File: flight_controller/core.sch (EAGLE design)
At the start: 113 parts, among them J1 MOLEX-2POS, J10 MOLEX-2POS, J11 MOLEX-2POS, J12 MOLEX-2POS, J13 MOLEX-3POS, J14 MOLEX-3POS, J15 MOLEX-4POS, J16 MOLEX-3POS, J17 MOLEX-3POS, J18 MOLEX-3POS, J19 MOLEX-3POS, J2 MOLEX-2POS, J20 MOLEX-4POS, J3 MOLEX-2POS, J4 MOLEX-2POS, J5 MOLEX-2POS, J6 MOLEX-2POS, J7 MOLEX-2POS, J8 MOLEX-2POS, J9 MOLEX-2POS, Q1 MMBT2222A, Q14 MMBT2222A, Q15 MMBT2222A, Q16 MMBT2222A, Q17 MMBT2222A, Q3 MMBT2222A, Q4 MMBT2222A, Q9 MMBT2222A, U1 MPU-6000QFN-24, U2 MEAS-MS5611, U3 USD-SOCKETNEW, U4 STM32F405, U5 MIC5219 3.3V

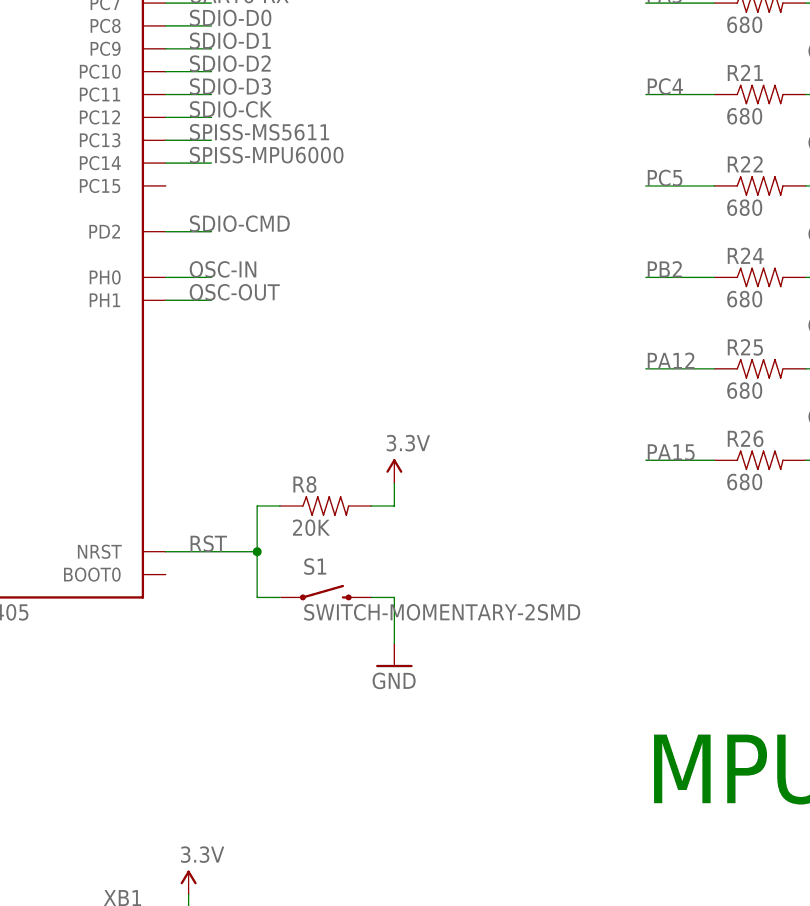
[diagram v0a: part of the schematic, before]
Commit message: Add oscillator.
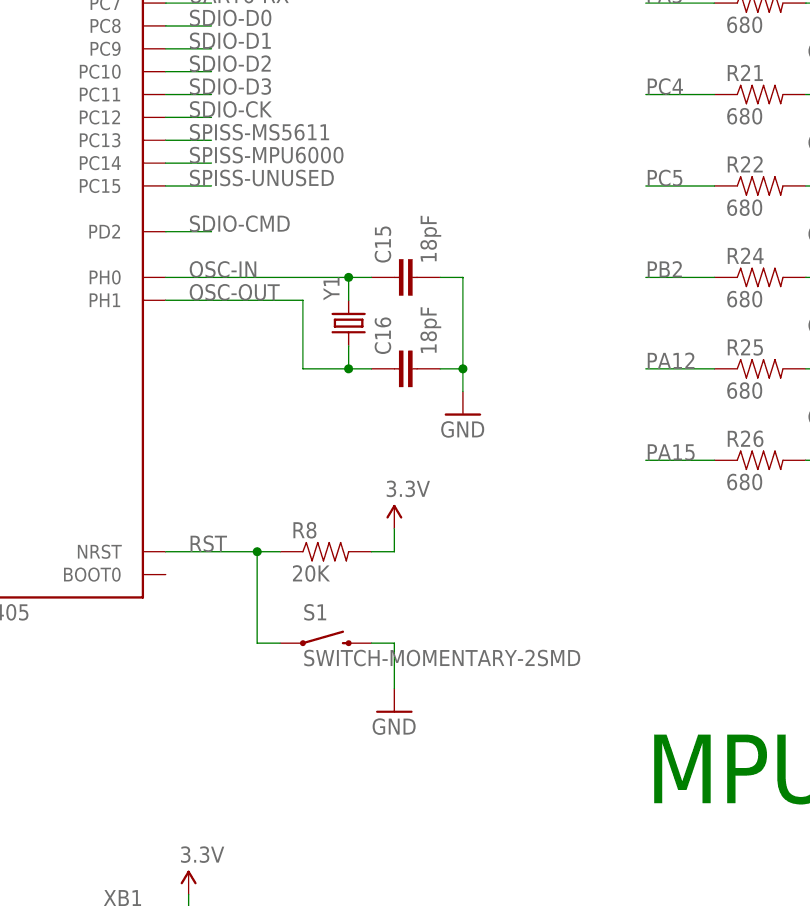
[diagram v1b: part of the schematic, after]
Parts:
- added C15, C16: 18pF, SparkFun-Capacitors:18PF-50V-5%(0603)
- added Y1: (no value), SparkFun-FreqCtrl:CRYSTAL5X3
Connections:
- net GND: now also C15.2, C16.2
- net OSC-IN: now also C15.1, Y1.2
- net OSC-OUT: now also C16.1, Y1.1
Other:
- moved on the sheet: R8, S1
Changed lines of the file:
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@@
 <part name="R37" library="SparkFun-Passives" deviceset="RESISTOR" device="0603-RES" value="20K"/>
 <part name="GND25" library="SparkFun-Aesthetics" deviceset="GND" device=""/>
+<part name="Y1" library="SparkFun-FreqCtrl" deviceset="CRYSTAL" device="5X3"/>
+<part name="C15" library="SparkFun-Capacitors" deviceset="18PF-50V-5%(0603)" device="" value="18pF"/>
+<part name="C16" library="SparkFun-Capacitors" deviceset="18PF-50V-5%(0603)" device="" value="18pF"/>
+<part name="GND26" library="SparkFun-Aesthetics" deviceset="GND" device=""/>
 </parts>
 <sheets>
@@
 <text x="53.34" y="-254" size="7.62" layer="91">MS5611</text>
 <text x="15.24" y="-208.28" size="7.62" layer="91">XBee</text>
-<text x="91.44" y="190.5" size="7.62" layer="98">TODO</text>
 <text x="88.9" y="111.76" size="7.62" layer="98">TODO</text>
 <text x="259.08" y="-523.24" size="7.62" layer="98">TODO</text>
@@
 <instance part="U4" gate=".GPIO" x="60.96" y="203.2"/>
 <instance part="U4" gate=".POWER" x="60.96" y="-154.94"/>
-<instance part="R8" gate="G$1" x="93.98" y="170.18"/>
+<instance part="R8" gate="G$1" x="93.98" y="165.1"/>
 <instance part="C8" gate="G$1" x="81.28" y="-104.14"/>
 <instance part="U5" gate="G$1" x="45.72" y="-91.44"/>
@@
 <instance part="R2" gate="G$1" x="269.24" y="-505.46" rot="R90"/>
 <instance part="SUPPLY16" gate="G$1" x="269.24" y="-474.98"/>
-<instance part="S1" gate="G$1" x="93.98" y="160.02"/>
-<instance part="SUPPLY17" gate="G$1" x="101.6" y="172.72"/>
-<instance part="GND12" gate="1" x="101.6" y="152.4"/>
+<instance part="S1" gate="G$1" x="93.98" y="154.94"/>
+<instance part="SUPPLY17" gate="G$1" x="101.6" y="167.64"/>
+<instance part="GND12" gate="1" x="101.6" y="147.32"/>
 <instance part="GND13" gate="1" x="160.02" y="167.64"/>
 <instance part="GND14" gate="1" x="208.28" y="157.48"/>
@@
 <instance part="R37" gate="G$1" x="177.8" y="-510.54"/>
 <instance part="GND25" gate="1" x="185.42" y="-518.16"/>
+<instance part="Y1" gate="G$1" x="96.52" y="190.5" rot="R90"/>
+<instance part="C15" gate="G$1" x="104.14" y="195.58" rot="R90"/>
+<instance part="C16" gate="G$1" x="104.14" y="185.42" rot="R90"/>
+<instance part="GND26" gate="1" x="109.22" y="180.34"/>
 </instances>
 <busses>
@@
 </segment>
 <segment>
-<wire x1="101.6" y1="160.02" x2="101.6" y2="154.94" width="0.1524" layer="91"/>
+<wire x1="101.6" y1="154.94" x2="101.6" y2="149.86" width="0.1524" layer="91"/>
 <pinref part="S1" gate="G$1" pin="2"/>
-<wire x1="101.6" y1="160.02" x2="99.06" y2="160.02" width="0.1524" layer="91"/>
+<wire x1="101.6" y1="154.94" x2="99.06" y2="154.94" width="0.1524" layer="91"/>
 <pinref part="GND12" gate="1" pin="GND"/>
 </segment>
@@
 <junction x="185.42" y="-510.54"/>
 </segment>
+<segment>
+<pinref part="C15" gate="G$1" pin="2"/>
+<pinref part="GND26" gate="1" pin="GND"/>
+<wire x1="106.68" y1="195.58" x2="109.22" y2="195.58" width="0.1524" layer="91"/>
+<wire x1="109.22" y1="195.58" x2="109.22" y2="185.42" width="0.1524" layer="91"/>
+<pinref part="C16" gate="G$1" pin="2"/>
+<wire x1="109.22" y1="185.42" x2="109.22" y2="182.88" width="0.1524" layer="91"/>
+<wire x1="106.68" y1="185.42" x2="109.22" y2="185.42" width="0.1524" layer="91"/>
+<junction x="109.22" y="185.42"/>
+</segment>
 </net>
 <net name="UART4-TX" class="0">
@@
 <wire x1="86.36" y1="165.1" x2="76.2" y2="165.1" width="0.1524" layer="91"/>
 <label x="78.74" y="165.1" size="1.778" layer="95"/>
-<wire x1="86.36" y1="170.18" x2="86.36" y2="165.1" width="0.1524" layer="91"/>
 <pinref part="S1" gate="G$1" pin="1"/>
-<wire x1="86.36" y1="165.1" x2="86.36" y2="160.02" width="0.1524" layer="91"/>
-<wire x1="86.36" y1="160.02" x2="88.9" y2="160.02" width="0.1524" layer="91"/>
+<wire x1="86.36" y1="165.1" x2="86.36" y2="154.94" width="0.1524" layer="91"/>
+<wire x1="86.36" y1="154.94" x2="88.9" y2="154.94" width="0.1524" layer="91"/>
 <junction x="86.36" y="165.1"/>
 <pinref part="R8" gate="G$1" pin="1"/>
-<wire x1="88.9" y1="170.18" x2="86.36" y2="170.18" width="0.1524" layer="91"/>
+<wire x1="88.9" y1="165.1" x2="86.36" y2="165.1" width="0.1524" layer="91"/>
 </segment>
 </net>
@@
 <segment>
 <pinref part="SUPPLY17" gate="G$1" pin="3.3V"/>
-<wire x1="101.6" y1="170.18" x2="101.6" y2="172.72" width="0.1524" layer="91"/>
+<wire x1="101.6" y1="165.1" x2="101.6" y2="167.64" width="0.1524" layer="91"/>
 <pinref part="R8" gate="G$1" pin="2"/>
-<wire x1="99.06" y1="170.18" x2="101.6" y2="170.18" width="0.1524" layer="91"/>
+<wire x1="99.06" y1="165.1" x2="101.6" y2="165.1" width="0.1524" layer="91"/>
 </segment>
 <segment>
@@
 <net name="OSC-IN" class="0">
 <segment>
-<wire x1="76.2" y1="195.58" x2="81.28" y2="195.58" width="0.1524" layer="91"/>
 <label x="78.74" y="195.58" size="1.778" layer="95"/>
 <pinref part="U4" gate=".GPIO" pin="PH0"/>
+<wire x1="76.2" y1="195.58" x2="96.52" y2="195.58" width="0.1524" layer="91"/>
+<pinref part="C15" gate="G$1" pin="1"/>
+<pinref part="Y1" gate="G$1" pin="2"/>
+<wire x1="96.52" y1="195.58" x2="99.06" y2="195.58" width="0.1524" layer="91"/>
+<wire x1="96.52" y1="193.04" x2="96.52" y2="195.58" width="0.1524" layer="91"/>
+<junction x="96.52" y="195.58"/>
 </segment>
 </net>
 <net name="OSC-OUT" class="0">
 <segment>
-<wire x1="76.2" y1="193.04" x2="81.28" y2="193.04" width="0.1524" layer="91"/>
 <label x="78.74" y="193.04" size="1.778" layer="95"/>
 <pinref part="U4" gate=".GPIO" pin="PH1"/>
+<wire x1="76.2" y1="193.04" x2="91.44" y2="193.04" width="0.1524" layer="91"/>
+<wire x1="91.44" y1="193.04" x2="91.44" y2="185.42" width="0.1524" layer="91"/>
+<wire x1="91.44" y1="185.42" x2="96.52" y2="185.42" width="0.1524" layer="91"/>
+<pinref part="C16" gate="G$1" pin="1"/>
+<pinref part="Y1" gate="G$1" pin="1"/>
+<wire x1="96.52" y1="185.42" x2="99.06" y2="185.42" width="0.1524" layer="91"/>
+<wire x1="96.52" y1="185.42" x2="96.52" y2="187.96" width="0.1524" layer="91"/>
+<junction x="96.52" y="185.42"/>
 </segment>
 </net>
@@
 </segment>
 </net>
+<net name="SPISS-UNUSED" class="0">
+<segment>
+<wire x1="76.2" y1="205.74" x2="81.28" y2="205.74" width="0.1524" layer="91"/>
+<label x="78.74" y="205.74" size="1.778" layer="95"/>
+</segment>
+</net>

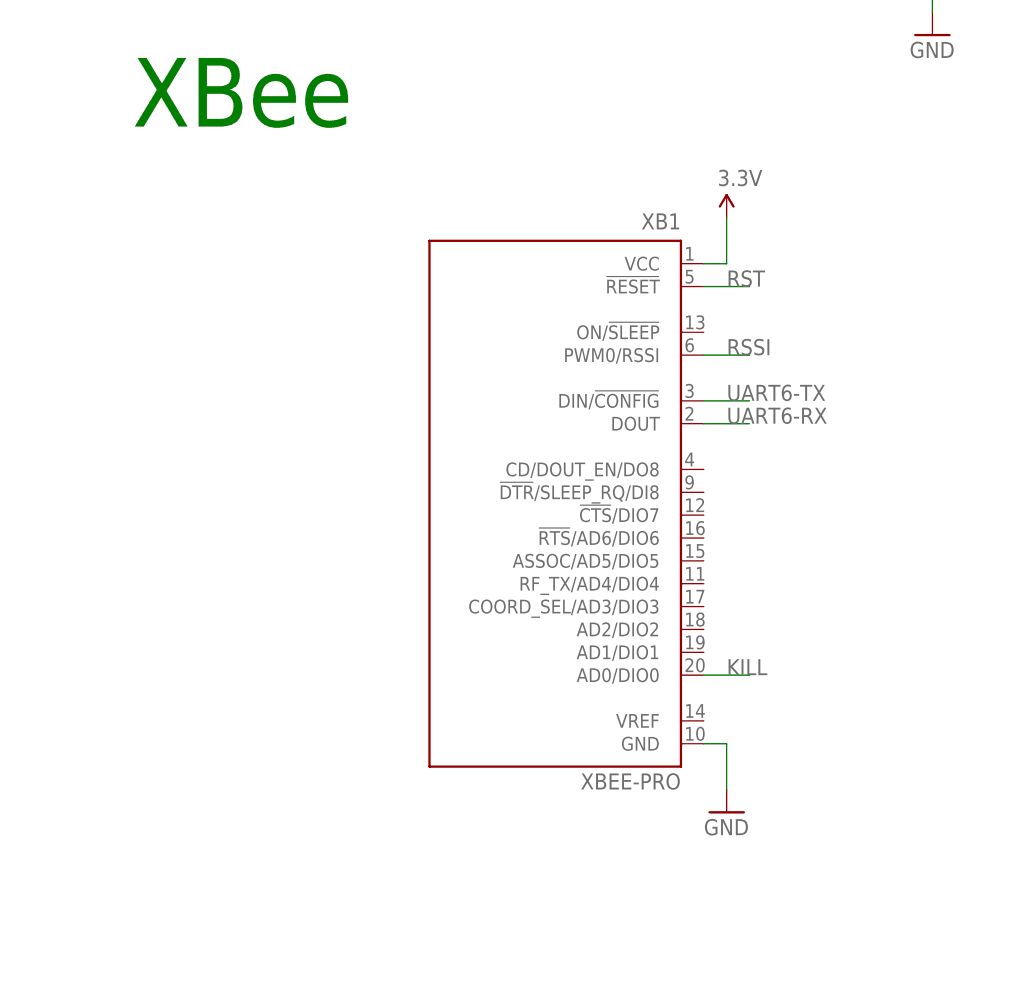
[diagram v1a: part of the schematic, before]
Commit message: Replace XBee headers with SMD variant.
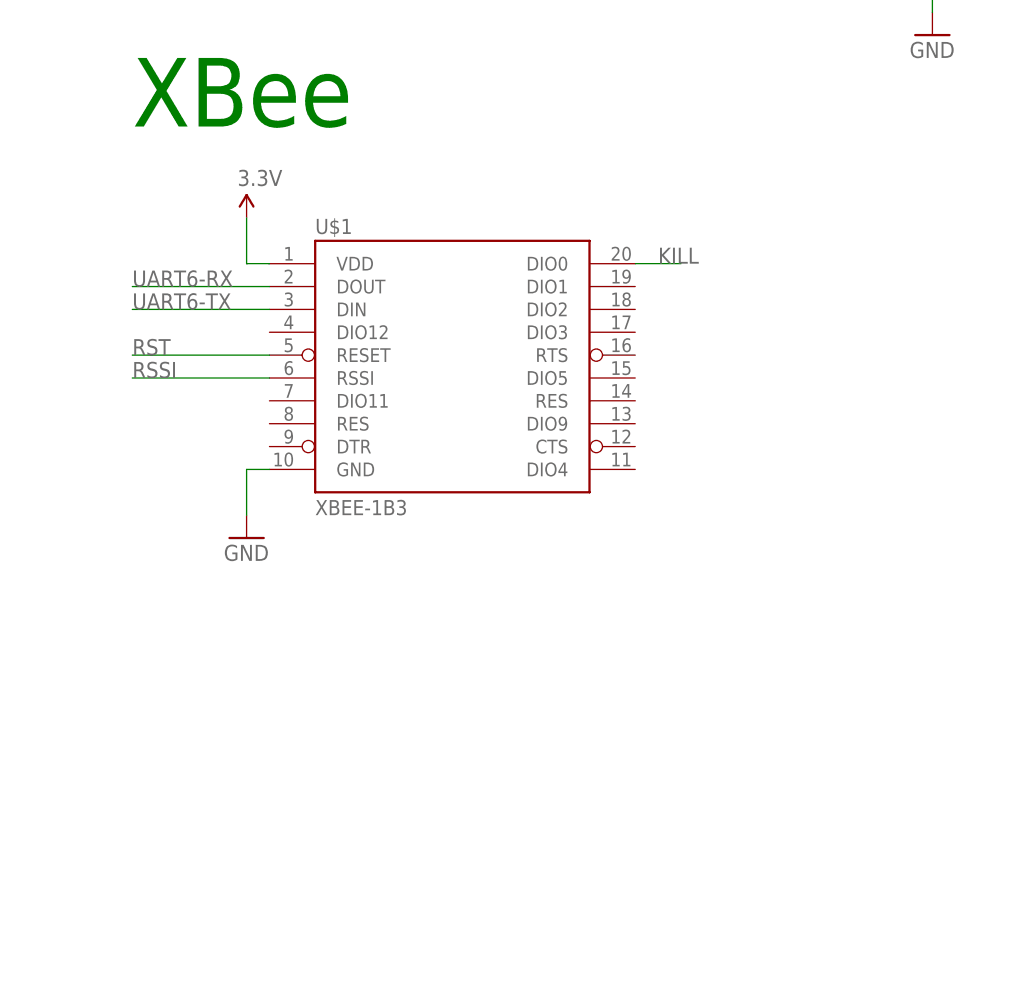
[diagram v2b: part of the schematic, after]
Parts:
- removed XB1: XBEE-PRO, maxstream:XBEE-PRO
- added U$1: XBEE-1B3, SparkFun-RF:XBEE-1B3
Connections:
- net 3.3V: now also U$1.VDD; no longer XB1.VCC
- net GND: now also U$1.GND; no longer XB1.GND
- net KILL: now also U$1.DIO0; no longer XB1.AD0/DIO0
- net RSSI: now also U$1.RSSI; no longer XB1.PWM0/RSSI
- net RST: now also U$1.RESET; no longer XB1.!RESET
- net UART6-RX: now also U$1.DOUT; no longer XB1.DOUT
- net UART6-TX: now also U$1.DIN; no longer XB1.DIN/!CONFIG
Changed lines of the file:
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@@
 </classes>
 <parts>
-<part name="XB1" library="maxstream" deviceset="XBEE" device="-PRO"/>
 <part name="SUPPLY1" library="SparkFun-Aesthetics" deviceset="3.3V" device=""/>
 <part name="GND1" library="SparkFun-Aesthetics" deviceset="GND" device=""/>
-<part name="SUPPLY3" library="SparkFun-Aesthetics" deviceset="3.3V" device=""/>
 <part name="GND2" library="SparkFun-Aesthetics" deviceset="GND" device=""/>
-<part name="GND3" library="SparkFun-Aesthetics" deviceset="GND" device=""/>
 <part name="SUPPLY4" library="SparkFun-Aesthetics" deviceset="5V" device=""/>
 <part name="GND4" library="SparkFun-Aesthetics" deviceset="GND" device=""/>
@@
 <part name="C16" library="SparkFun-Capacitors" deviceset="18PF-50V-5%(0603)" device="" value="18pF"/>
 <part name="GND26" library="SparkFun-Aesthetics" deviceset="GND" device=""/>
+<part name="U$1" library="SparkFun-RF" deviceset="XBEE-1" device="B3"/>
+<part name="GND27" library="SparkFun-Aesthetics" deviceset="GND" device=""/>
+<part name="SUPPLY11" library="SparkFun-Aesthetics" deviceset="3.3V" device=""/>
 </parts>
 <sheets>
@@
 </plain>
 <instances>
-<instance part="XB1" gate="G$1" x="60.96" y="96.52" rot="MR0"/>
 <instance part="SUPPLY1" gate="G$1" x="17.78" y="-144.78"/>
 <instance part="GND1" gate="1" x="60.96" y="-182.88"/>
-<instance part="SUPPLY3" gate="G$1" x="78.74" y="127"/>
 <instance part="GND2" gate="1" x="187.96" y="-447.04"/>
-<instance part="GND3" gate="1" x="78.74" y="60.96"/>
 <instance part="SUPPLY4" gate="G$1" x="187.96" y="-414.02"/>
 <instance part="GND4" gate="1" x="33.02" y="-482.6"/>
@@
 <instance part="C16" gate="G$1" x="104.14" y="185.42" rot="R90"/>
 <instance part="GND26" gate="1" x="109.22" y="180.34"/>
+<instance part="U$1" gate="G$1" x="48.26" y="111.76"/>
+<instance part="GND27" gate="1" x="25.4" y="91.44"/>
+<instance part="SUPPLY11" gate="G$1" x="25.4" y="127"/>
 </instances>
 <busses>
@@
 <label x="213.36" y="-416.56" size="1.778" layer="95"/>
 <pinref part="J20" gate="G$1" pin="2"/>
-</segment>
-<segment>
-<pinref part="XB1" gate="G$1" pin="GND"/>
-<wire x1="76.2" y1="68.58" x2="78.74" y2="68.58" width="0.1524" layer="91"/>
-<wire x1="78.74" y1="68.58" x2="78.74" y2="63.5" width="0.1524" layer="91"/>
-<pinref part="GND3" gate="1" pin="GND"/>
 </segment>
 <segment>
@@
 <junction x="109.22" y="185.42"/>
 </segment>
+<segment>
+<pinref part="U$1" gate="G$1" pin="GND"/>
+<wire x1="27.94" y1="99.06" x2="25.4" y2="99.06" width="0.1524" layer="91"/>
+<wire x1="25.4" y1="99.06" x2="25.4" y2="93.98" width="0.1524" layer="91"/>
+<pinref part="GND27" gate="1" pin="GND"/>
+</segment>
 </net>
 <net name="UART4-TX" class="0">
@@
 <label x="213.36" y="-414.02" size="1.778" layer="95"/>
 <pinref part="J20" gate="G$1" pin="1"/>
-</segment>
-<segment>
-<pinref part="XB1" gate="G$1" pin="!RESET"/>
-<wire x1="76.2" y1="119.38" x2="81.28" y2="119.38" width="0.1524" layer="91"/>
-<label x="78.74" y="119.38" size="1.778" layer="95"/>
 </segment>
 <segment>
@@
 <pinref part="R8" gate="G$1" pin="1"/>
 <wire x1="88.9" y1="165.1" x2="86.36" y2="165.1" width="0.1524" layer="91"/>
+</segment>
+<segment>
+<pinref part="U$1" gate="G$1" pin="RESET"/>
+<wire x1="27.94" y1="111.76" x2="12.7" y2="111.76" width="0.1524" layer="91"/>
+<label x="12.7" y="111.76" size="1.778" layer="95"/>
 </segment>
 </net>
@@
 </segment>
 <segment>
-<pinref part="XB1" gate="G$1" pin="VCC"/>
-<wire x1="76.2" y1="121.92" x2="78.74" y2="121.92" width="0.1524" layer="91"/>
-<wire x1="78.74" y1="121.92" x2="78.74" y2="127" width="0.1524" layer="91"/>
-<pinref part="SUPPLY3" gate="G$1" pin="3.3V"/>
-</segment>
-<segment>
 <wire x1="193.04" y1="-436.88" x2="187.96" y2="-436.88" width="0.1524" layer="91"/>
 <wire x1="193.04" y1="-421.64" x2="187.96" y2="-421.64" width="0.1524" layer="91"/>
@@
 <pinref part="C9" gate="G$1" pin="1"/>
 </segment>
+<segment>
+<pinref part="U$1" gate="G$1" pin="VDD"/>
+<wire x1="27.94" y1="121.92" x2="25.4" y2="121.92" width="0.1524" layer="91"/>
+<wire x1="25.4" y1="121.92" x2="25.4" y2="127" width="0.1524" layer="91"/>
+<pinref part="SUPPLY11" gate="G$1" pin="3.3V"/>
+</segment>
 </net>
 <net name="KILL" class="0">
-<segment>
-<label x="78.74" y="76.2" size="1.778" layer="95"/>
-<pinref part="XB1" gate="G$1" pin="AD0/DIO0"/>
-<wire x1="81.28" y1="76.2" x2="76.2" y2="76.2" width="0.1524" layer="91"/>
-</segment>
 <segment>
 <pinref part="R28" gate="G$1" pin="1"/>
@@
 <label x="388.62" y="246.38" size="1.778" layer="95"/>
 </segment>
+<segment>
+<wire x1="73.66" y1="121.92" x2="68.58" y2="121.92" width="0.1524" layer="91"/>
+<label x="71.12" y="121.92" size="1.778" layer="95"/>
+<pinref part="U$1" gate="G$1" pin="DIO0"/>
+</segment>
 </net>
 <net name="RSSI" class="0">
-<segment>
-<pinref part="XB1" gate="G$1" pin="PWM0/RSSI"/>
-<wire x1="76.2" y1="111.76" x2="81.28" y2="111.76" width="0.1524" layer="91"/>
-<label x="78.74" y="111.76" size="1.778" layer="95"/>
-</segment>
 <segment>
 <pinref part="R27" gate="G$1" pin="1"/>
 <wire x1="233.68" y1="215.9" x2="218.44" y2="215.9" width="0.1524" layer="91"/>
 <label x="218.44" y="215.9" size="1.778" layer="95"/>
+</segment>
+<segment>
+<pinref part="U$1" gate="G$1" pin="RSSI"/>
+<wire x1="27.94" y1="109.22" x2="12.7" y2="109.22" width="0.1524" layer="91"/>
+<label x="12.7" y="109.22" size="1.778" layer="95"/>
 </segment>
 </net>
@@
 </segment>
 <segment>
-<pinref part="XB1" gate="G$1" pin="DIN/!CONFIG"/>
-<wire x1="76.2" y1="106.68" x2="81.28" y2="106.68" width="0.1524" layer="91"/>
-<label x="78.74" y="106.68" size="1.778" layer="95"/>
-</segment>
-<segment>
 <wire x1="35.56" y1="-558.8" x2="15.24" y2="-558.8" width="0.1524" layer="91"/>
 <label x="15.24" y="-558.8" size="1.778" layer="95"/>
@@
 <label x="218.44" y="236.22" size="1.778" layer="95"/>
 </segment>
+<segment>
+<pinref part="U$1" gate="G$1" pin="DIN"/>
+<wire x1="27.94" y1="116.84" x2="12.7" y2="116.84" width="0.1524" layer="91"/>
+<label x="12.7" y="116.84" size="1.778" layer="95"/>
+</segment>
 </net>
 <net name="UART6-RX" class="0">
@@
 </segment>
 <segment>
-<pinref part="XB1" gate="G$1" pin="DOUT"/>
-<wire x1="76.2" y1="104.14" x2="81.28" y2="104.14" width="0.1524" layer="91"/>
-<label x="78.74" y="104.14" size="1.778" layer="95"/>
-</segment>
-<segment>
 <wire x1="35.56" y1="-561.34" x2="15.24" y2="-561.34" width="0.1524" layer="91"/>
 <label x="15.24" y="-561.34" size="1.778" layer="95"/>
@@
 <label x="218.44" y="226.06" size="1.778" layer="95"/>
 </segment>
-</net>
+<segment>
+<pinref part="U$1" gate="G$1" pin="DOUT"/>
+<wire x1="27.94" y1="119.38" x2="12.7" y2="119.38" width="0.1524" layer="91"/>
+<label x="12.7" y="119.38" size="1.778" layer="95"/>
+</segment>
+</net>

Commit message: Reassign and rename UART buses to XBee and GPS.
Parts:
- J18: value MOLEX-3POS -> MOLEX-4POS; device aerial:MOLEX-3POS -> aerial:MOLEX-4POS
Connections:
- removed net UART2-RX: J17.2, U4.GPIO.PA3
- removed net UART2-TX: J17.1, U4.GPIO.PA2
- removed net UART6-RX: J19.2, R30.1, U$1.DOUT, U4.GPIO.PC7
- removed net UART6-TX: J19.1, R29.1, U$1.DIN, U4.GPIO.PC6
- new net SPISS-UNUSED: U4.GPIO.PC15
- new net UART2-RX-XBEE: J17.2, R30.1, U$1.DOUT, U4.GPIO.PA3
- new net UART2-TX-XBEE: J17.1, R29.1, U$1.DIN, U4.GPIO.PA2
- new net UART6-RX-GPS: J18.3, U4.GPIO.PC7
- new net UART6-TX-GPS: J18.2, U4.GPIO.PC6
- net 5V: now also J18.1
- net GND: now also J18.4, R13.1; no longer J18.3, R11.2
- net KILL-BASE: now also R11.2; no longer R13.1
- net RST: now also U4.GPIO.NRST
- net UART4-RX: now also J19.2; no longer J18.2
- net UART4-TX: now also J19.1; no longer J18.1
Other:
- moved on the sheet: C12, C15, C16, C19, J17, J19, LED1, LED10, LED11, LED12, LED13, LED14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
